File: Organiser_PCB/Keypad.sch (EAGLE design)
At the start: 54 parts, among them IC1 MCP23017SO

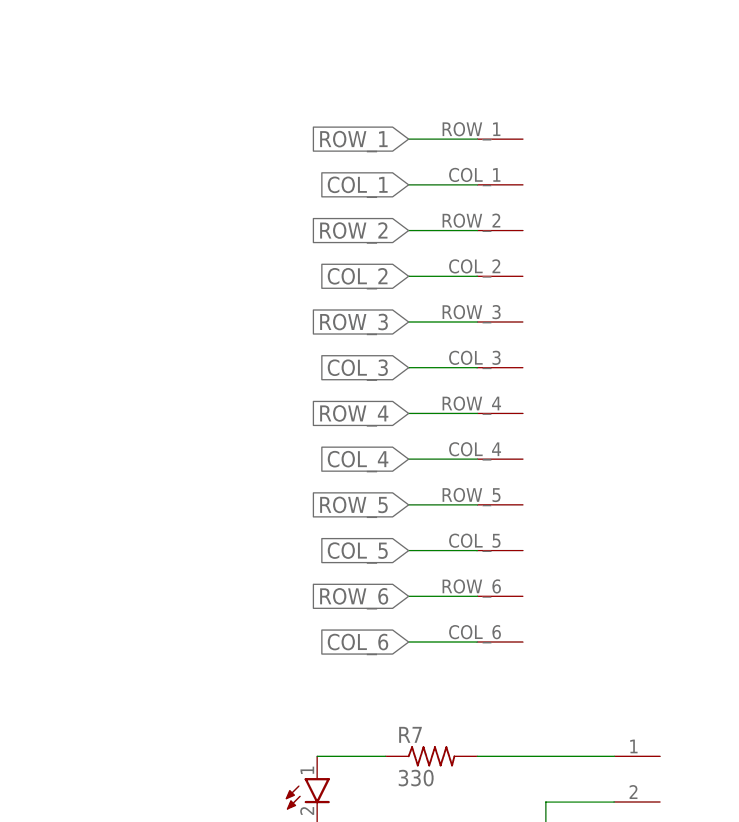
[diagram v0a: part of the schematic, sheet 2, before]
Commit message: Changed LCD to use MCP23S17 with SPI interface Reduced example execution time to draw on LCD from 4 seconds down to 251 ms (I2C to SPI)
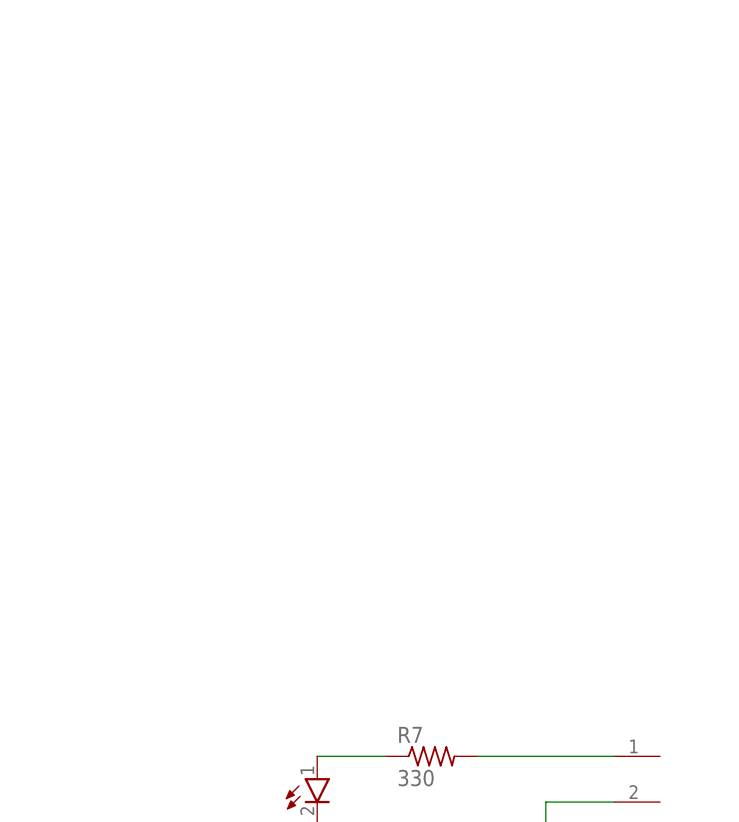
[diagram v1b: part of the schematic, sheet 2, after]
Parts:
- removed U$37: HEADER-1X12-KEYPAD, teelsys-0.2:HEADER-1X12-KEYPAD
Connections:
- net COL_1: no longer U$37.COL_1
- net COL_2: no longer U$37.COL_2
- net COL_3: no longer U$37.COL_3
- net COL_4: no longer U$37.COL_4
- net COL_5: no longer U$37.COL_5
- net COL_6: no longer U$37.COL_6
- net ROW_1: no longer U$37.ROW_1
- net ROW_2: no longer U$37.ROW_2
- net ROW_3: no longer U$37.ROW_3
- net ROW_4: no longer U$37.ROW_4
- net ROW_5: no longer U$37.ROW_5
- net ROW_6: no longer U$37.ROW_6
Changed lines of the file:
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@@
 <part name="SUPPLY3" library="supply2" deviceset="GND" device=""/>
 <part name="U$73" library="teelsys-0.2" deviceset="LCD_CFAL12832A022" device=""/>
-<part name="U$37" library="teelsys-0.2" deviceset="HEADER-1X12-KEYPAD" device=""/>
 <part name="U$38" library="teelsys-0.2" deviceset="HEADER-1X18-LCD" device=""/>
 <part name="LED1" library="teelsys-0.2" deviceset="LED" device="" value="RED"/>
@@
 <instance part="SUPPLY3" gate="GND" x="20.32" y="30.48"/>
 <instance part="U$73" gate="G$1" x="30.48" y="12.7"/>
-<instance part="U$37" gate="G$1" x="205.74" y="132.08"/>
 <instance part="U$38" gate="G$1" x="76.2" y="66.04" rot="R90"/>
 <instance part="LED1" gate="G$1" x="187.96" y="86.36"/>
@@
 <net name="ROW_1" class="0">
 <segment>
-<pinref part="U$37" gate="G$1" pin="ROW_1"/>
-<wire x1="205.74" y1="160.02" x2="198.12" y2="160.02" width="0.1524" layer="91"/>
-<label x="198.12" y="160.02" size="1.778" layer="95" rot="R180" xref="yes"/>
-</segment>
-<segment>
 <pinref part="IC1" gate="G$1" pin="GPA0"/>
 <wire x1="96.52" y1="162.56" x2="104.14" y2="162.56" width="0.1524" layer="91"/>
@@
 <net name="COL_1" class="0">
 <segment>
-<pinref part="U$37" gate="G$1" pin="COL_1"/>
-<wire x1="205.74" y1="154.94" x2="198.12" y2="154.94" width="0.1524" layer="91"/>
-<label x="198.12" y="154.94" size="1.778" layer="95" rot="R180" xref="yes"/>
-</segment>
-<segment>
 <pinref part="IC1" gate="G$1" pin="GPB0"/>
 <wire x1="96.52" y1="139.7" x2="104.14" y2="139.7" width="0.1524" layer="91"/>
@@
 <net name="ROW_2" class="0">
 <segment>
-<pinref part="U$37" gate="G$1" pin="ROW_2"/>
-<wire x1="205.74" y1="149.86" x2="198.12" y2="149.86" width="0.1524" layer="91"/>
-<label x="198.12" y="149.86" size="1.778" layer="95" rot="R180" xref="yes"/>
-</segment>
-<segment>
 <pinref part="IC1" gate="G$1" pin="GPA1"/>
 <wire x1="96.52" y1="160.02" x2="121.92" y2="160.02" width="0.1524" layer="91"/>
@@
 <net name="COL_2" class="0">
 <segment>
-<pinref part="U$37" gate="G$1" pin="COL_2"/>
-<wire x1="205.74" y1="144.78" x2="198.12" y2="144.78" width="0.1524" layer="91"/>
-<label x="198.12" y="144.78" size="1.778" layer="95" rot="R180" xref="yes"/>
-</segment>
-<segment>
 <pinref part="IC1" gate="G$1" pin="GPB1"/>
 <wire x1="96.52" y1="137.16" x2="121.92" y2="137.16" width="0.1524" layer="91"/>
@@
 <net name="ROW_3" class="0">
 <segment>
-<pinref part="U$37" gate="G$1" pin="ROW_3"/>
-<wire x1="205.74" y1="139.7" x2="198.12" y2="139.7" width="0.1524" layer="91"/>
-<label x="198.12" y="139.7" size="1.778" layer="95" rot="R180" xref="yes"/>
-</segment>
-<segment>
 <pinref part="IC1" gate="G$1" pin="GPA2"/>
 <wire x1="96.52" y1="157.48" x2="104.14" y2="157.48" width="0.1524" layer="91"/>
@@
 <net name="COL_3" class="0">
 <segment>
-<pinref part="U$37" gate="G$1" pin="COL_3"/>
-<wire x1="205.74" y1="134.62" x2="198.12" y2="134.62" width="0.1524" layer="91"/>
-<label x="198.12" y="134.62" size="1.778" layer="95" rot="R180" xref="yes"/>
-</segment>
-<segment>
 <pinref part="IC1" gate="G$1" pin="GPB2"/>
 <wire x1="96.52" y1="134.62" x2="104.14" y2="134.62" width="0.1524" layer="91"/>
@@
 <net name="ROW_4" class="0">
 <segment>
-<pinref part="U$37" gate="G$1" pin="ROW_4"/>
-<wire x1="205.74" y1="129.54" x2="198.12" y2="129.54" width="0.1524" layer="91"/>
-<label x="198.12" y="129.54" size="1.778" layer="95" rot="R180" xref="yes"/>
-</segment>
-<segment>
 <pinref part="IC1" gate="G$1" pin="GPA3"/>
 <wire x1="96.52" y1="154.94" x2="121.92" y2="154.94" width="0.1524" layer="91"/>
@@
 <net name="COL_4" class="0">
 <segment>
-<pinref part="U$37" gate="G$1" pin="COL_4"/>
-<wire x1="205.74" y1="124.46" x2="198.12" y2="124.46" width="0.1524" layer="91"/>
-<label x="198.12" y="124.46" size="1.778" layer="95" rot="R180" xref="yes"/>
-</segment>
-<segment>
 <pinref part="IC1" gate="G$1" pin="GPB3"/>
 <wire x1="96.52" y1="132.08" x2="121.92" y2="132.08" width="0.1524" layer="91"/>
@@
 <net name="ROW_5" class="0">
 <segment>
-<pinref part="U$37" gate="G$1" pin="ROW_5"/>
-<wire x1="205.74" y1="119.38" x2="198.12" y2="119.38" width="0.1524" layer="91"/>
-<label x="198.12" y="119.38" size="1.778" layer="95" rot="R180" xref="yes"/>
-</segment>
-<segment>
 <pinref part="IC1" gate="G$1" pin="GPA4"/>
 <wire x1="96.52" y1="152.4" x2="104.14" y2="152.4" width="0.1524" layer="91"/>
@@
 <net name="COL_5" class="0">
 <segment>
-<pinref part="U$37" gate="G$1" pin="COL_5"/>
-<wire x1="205.74" y1="114.3" x2="198.12" y2="114.3" width="0.1524" layer="91"/>
-<label x="198.12" y="114.3" size="1.778" layer="95" rot="R180" xref="yes"/>
-</segment>
-<segment>
 <pinref part="IC1" gate="G$1" pin="GPB4"/>
 <wire x1="96.52" y1="129.54" x2="104.14" y2="129.54" width="0.1524" layer="91"/>
@@
 <net name="ROW_6" class="0">
 <segment>
-<pinref part="U$37" gate="G$1" pin="ROW_6"/>
-<wire x1="205.74" y1="109.22" x2="198.12" y2="109.22" width="0.1524" layer="91"/>
-<label x="198.12" y="109.22" size="1.778" layer="95" rot="R180" xref="yes"/>
-</segment>
-<segment>
 <pinref part="IC1" gate="G$1" pin="GPA5"/>
 <wire x1="96.52" y1="149.86" x2="121.92" y2="149.86" width="0.1524" layer="91"/>
@@
 <net name="COL_6" class="0">
 <segment>
-<pinref part="U$37" gate="G$1" pin="COL_6"/>
-<wire x1="205.74" y1="104.14" x2="198.12" y2="104.14" width="0.1524" layer="91"/>
-<label x="198.12" y="104.14" size="1.778" layer="95" rot="R180" xref="yes"/>
-</segment>
-<segment>
 <pinref part="IC1" gate="G$1" pin="GPB5"/>
